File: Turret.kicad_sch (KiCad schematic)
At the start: 24 parts, among them J1 Conn_01x04_Pin, J12 Conn_01x02_Pin, J13 Conn_01x04_Pin, J14 Conn_01x04_Pin, J15 Conn_01x08_Pin, J2 Conn_01x02_Pin, J20 Conn_01x02_Pin, J21 Conn_01x02_Pin, J3 Conn_01x02_Pin, J4 Conn_01x02_Pin, J5 Conn_01x04_Pin, J6 Conn_01x02_Pin, J7 Conn_01x02_Pin, J8 Conn_01x02_Pin, J9 Conn_01x02_Pin

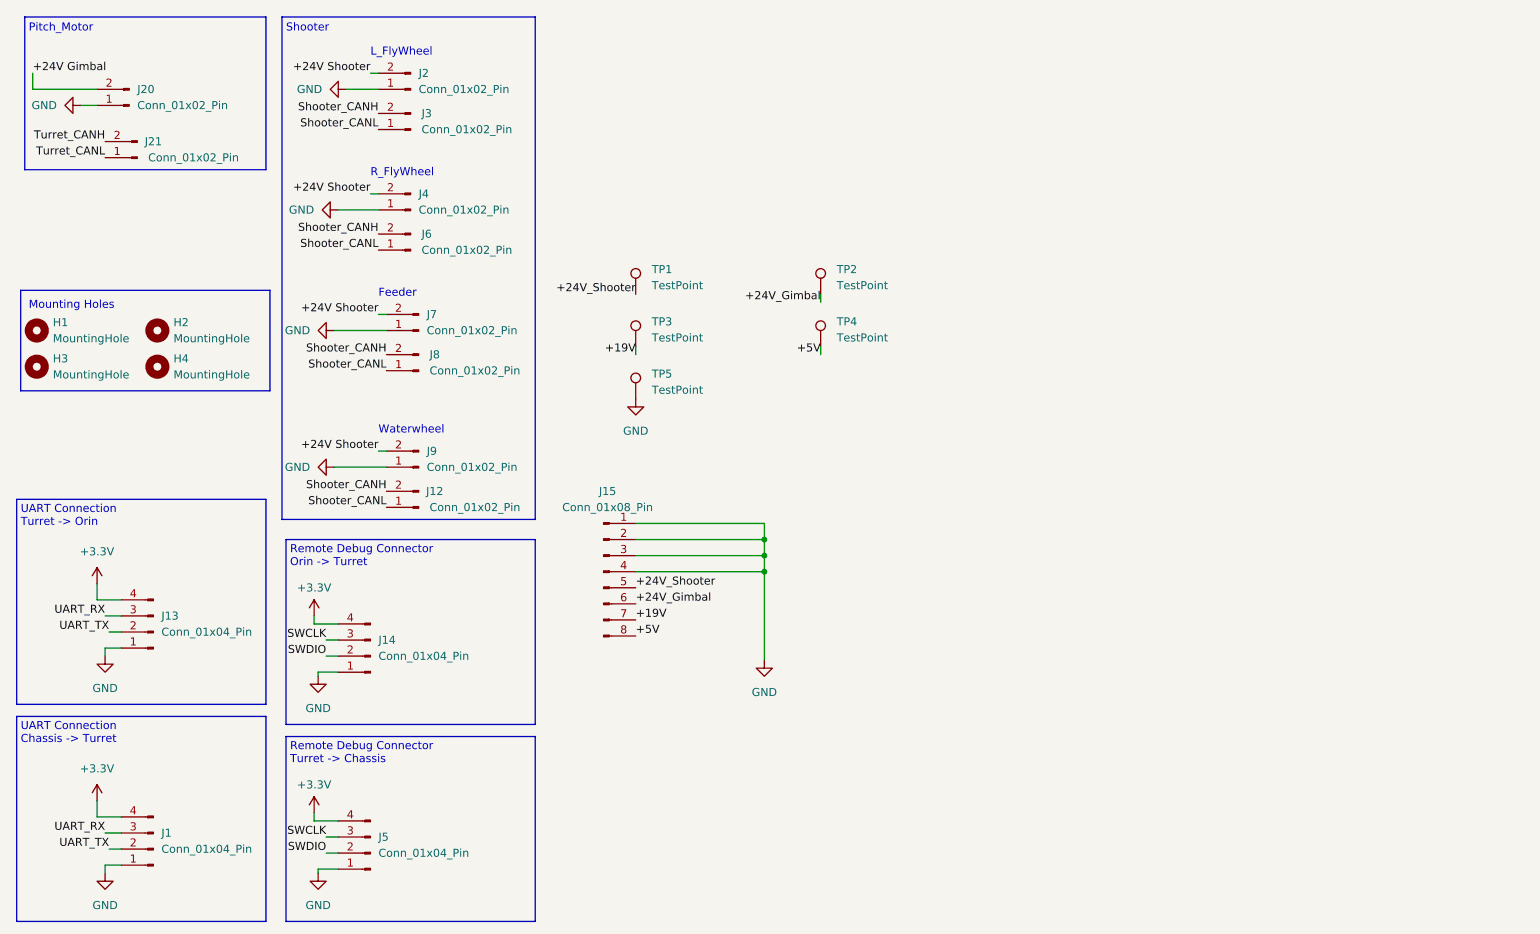
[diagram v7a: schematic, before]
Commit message: Fix CAN and change schematic
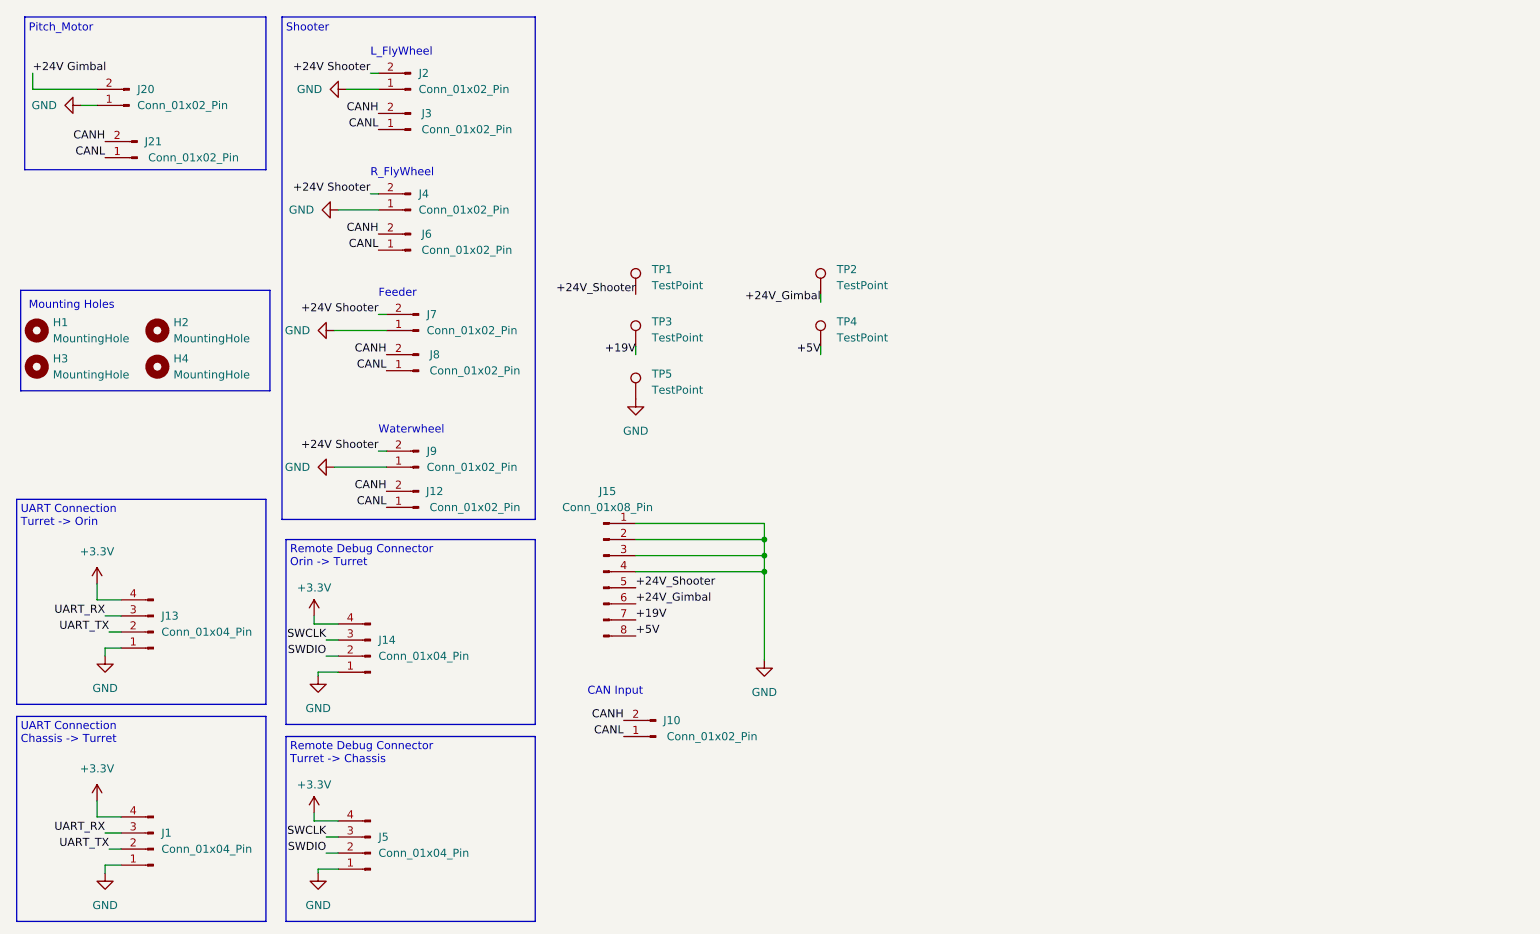
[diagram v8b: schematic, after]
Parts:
- added J10: Conn_01x02_Pin, Connector_JST:JST_GH_BM02B-GHS-TBT_1x02-1MP_P1.25mm_Vertical, symbol Connector:Conn_01x02_Pin
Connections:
- net Turret_CANH is gone; now on net CANH: J21.2 (Pin_2)
- net Turret_CANL is gone; now on net CANL: J21.1 (Pin_1)
- net Shooter_CANH renamed CANH
- net CANH: now also J10.2 (Pin_2)
- net Shooter_CANL renamed CANL
- net CANL: now also J10.1 (Pin_1)
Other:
- note added: "CAN Input"
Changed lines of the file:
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@@
+    (effects (font (size 1.27 1.27)) (justify left bottom))
+  )
+  (text "CAN Input" (at 111.76 134.62 0)
     (effects (font (size 1.27 1.27)) (justify left bottom))
   )
@@
     (effects (font (size 1.27 1.27)) (justify left bottom))
   )
-  (label "Shooter_CANL" (at 78.74 45.085 180) (fields_autoplaced)
-    (effects (font (size 1.27 1.27)) (justify right bottom))
-  )
-  (label "Shooter_CANL" (at 80.01 83.185 180) (fields_autoplaced)
+  (label "CANL" (at 78.74 45.085 180) (fields_autoplaced)
+    (effects (font (size 1.27 1.27)) (justify right bottom))
+  )
+  (label "CANL" (at 80.01 83.185 180) (fields_autoplaced)
+    (effects (font (size 1.27 1.27)) (justify right bottom))
+  )
+  (label "CANL" (at 117.475 140.97 180) (fields_autoplaced)
     (effects (font (size 1.27 1.27)) (justify right bottom))
   )
@@
     (effects (font (size 1.27 1.27)) (justify right bottom))
   )
-  (label "Turret_CANH" (at 35.56 46.99 180) (fields_autoplaced)
+  (label "CANH" (at 35.56 46.99 180) (fields_autoplaced)
     (effects (font (size 1.27 1.27)) (justify right bottom))
   )
@@
     (effects (font (size 1.27 1.27)) (justify right bottom))
   )
-  (label "Shooter_CANH" (at 80.01 80.645 180) (fields_autoplaced)
-    (effects (font (size 1.27 1.27)) (justify right bottom))
-  )
-  (label "Shooter_CANH" (at 78.74 42.545 180) (fields_autoplaced)
+  (label "CANH" (at 117.475 138.43 180) (fields_autoplaced)
+    (effects (font (size 1.27 1.27)) (justify right bottom))
+  )
+  (label "CANH" (at 80.01 80.645 180) (fields_autoplaced)
+    (effects (font (size 1.27 1.27)) (justify right bottom))
+  )
+  (label "CANH" (at 78.74 42.545 180) (fields_autoplaced)
     (effects (font (size 1.27 1.27)) (justify right bottom))
   )
@@
     (effects (font (size 1.27 1.27)) (justify right bottom))
   )
-  (label "Turret_CANL" (at 35.56 49.53 180) (fields_autoplaced)
-    (effects (font (size 1.27 1.27)) (justify right bottom))
-  )
-  (label "Shooter_CANL" (at 78.74 64.135 180) (fields_autoplaced)
+  (label "CANL" (at 35.56 49.53 180) (fields_autoplaced)
+    (effects (font (size 1.27 1.27)) (justify right bottom))
+  )
+  (label "CANL" (at 78.74 64.135 180) (fields_autoplaced)
     (effects (font (size 1.27 1.27)) (justify right bottom))
   )
@@
     (effects (font (size 1.27 1.27)) (justify right bottom))
   )
-  (label "Shooter_CANH" (at 80.01 102.235 180) (fields_autoplaced)
+  (label "CANH" (at 80.01 102.235 180) (fields_autoplaced)
     (effects (font (size 1.27 1.27)) (justify right bottom))
   )
@@
     (effects (font (size 1.27 1.27)) (justify right bottom))
   )
-  (label "Shooter_CANH" (at 78.74 61.595 180) (fields_autoplaced)
+  (label "CANH" (at 78.74 61.595 180) (fields_autoplaced)
     (effects (font (size 1.27 1.27)) (justify right bottom))
   )
@@
     (effects (font (size 1.27 1.27)) (justify right bottom))
   )
-  (label "Shooter_CANL" (at 80.01 104.775 180) (fields_autoplaced)
+  (label "CANL" (at 80.01 104.775 180) (fields_autoplaced)
     (effects (font (size 1.27 1.27)) (justify right bottom))
   )
@@
         )
       )
+    )
+  )
+  (symbol (lib_id "Connector:Conn_01x02_Pin") (at 122.555 140.97 180) (unit 1)
+    (in_bom yes) (on_board yes) (dnp no)
+    (property "Reference" "J10" (at 125.095 138.43 0)
+      (effects (font (size 1.27 1.27)))
+    )
+    (property "Value" "Conn_01x02_Pin" (at 131.445 140.97 0)
+      (effects (font (size 1.27 1.27)))
+    )
+    (property "Footprint" "Connector_JST:JST_GH_BM02B-GHS-TBT_1x02-1MP_P1.25mm_Vertical" (at 122.555 140.97 0)
+      (effects (font (size 1.27 1.27)) hide)
+    )
+    (property "Datasheet" "~" (at 122.555 140.97 0)
+      (effects (font (size 1.27 1.27)) hide)
+    )
+    (pin "1")
+    (pin "2")
+    (instances
+      (project "Turret"
+        (path "/84905b3c-2997-4e61-b373-c0062fb72371"
+          (reference "J10") (unit 1)
+        )
+      )
